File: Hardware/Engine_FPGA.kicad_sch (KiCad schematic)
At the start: 9 parts, among them J12 Conn_02x05_Odd_Even, SW1 SW_DS01-254, U16 AT40K10-2DQU, U2 AT40K10-2DQU

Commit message: Started fixing many small issues.
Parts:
- removed U16: AT40K10-2DQU, Package_QFP:PQFP-208_28x28mm_P0.5mm, symbol LRJ-parts:AT40K10-2DQU
- added U3: AT40K10-2DQU, Package_QFP:PQFP-208_28x28mm_P0.5mm, symbol LRJ-parts:AT40K10-2DQU
- renumbered J12 to J-fpga1
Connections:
- net ~{MCAS0} is gone; now on net ~{RFSH}: U2.111 (IO99)
- net ~{MCAS1} is gone; now on net ~{WAIT}: U2.112 (IO100)
- net ~{MCAS2} is gone; now on net ~{M1}: U2.114 (IO104)
- net ~{MCAS3} is gone; now on net ~{IORQ}: U2.115 (IO105)
- net ~{MRAS0} is gone; now on net Z80M: U2.116 (IO106)
- net ~{MRAS1} is gone; now on net ~{SLTSL1}: U2.117 (IO107)
- net ~{MRAS2} is gone; now on net ~{REDWC}: U2.163 (IO147)
- net ~{MRAS3} is gone; now on net ~{INDEX}: U2.164 (IO148)
- net ~{MREQ} is gone; now on net ~{STROBE}: U2.93 (IO89)
- net A17: now also U3.161 (IO145/A0); no longer U2.5 (IO2/A17)
- net A18: now also U3.162 (IO146/GCK7/A1); no longer U2.8 (IO5/A18)
- net A19: now also U3.165 (IO149/~{CS1}/A2); no longer U2.9 (IO6/A19)
- net A20: now also U3.166 (IO150/A3); no longer U2.17 (IO15/A20)
- net A21: now also U3.174 (IO161/A4); no longer U2.18 (IO16/A21)
- net A22: now also U3.175 (IO162/A5); no longer U2.23 (IO23/A22)
- net A23: now also U3.180 (IO167/A6); no longer U2.24 (IO24/A23)
- net A24: now also U3.181 (IO168/A7)
- net A25: now also U3.184 (IO169/A8)
- net A26: now also U3.185 (IO170/A9)
- net A27: now also U3.190 (IO175/A10)
- net A28: now also U3.191 (IO176/A11)
- net A29: now also U3.199 (IO185/A12)
- net A30: now also U3.200 (IO186/A13)
- net A31: now also U3.203 (IO191/A14)
- net CAPS_LED: now also U2.28 (IO26); no longer U2.32 (IO30)
- net CC1/HPD: now also U3.24 (IO24/A23)
- net CCLK: now also U3.153 (CCLK)
- net COL0: now also U2.32 (IO30); no longer U2.38 (IO39)
- net COL1: now also U2.33 (IO33); no longer U2.39 (IO40)
- net COL2: now also U2.34 (IO34); no longer U2.40 (IO41)
- net COL3: now also U2.35 (IO35); no longer U2.41 (IO42)
- net COL4: now also U2.38 (IO39); no longer U2.42 (IO43)
- net COL5: now also U2.39 (IO40); no longer U2.43 (IO44)
- net COL6: now also U2.40 (IO41); no longer U2.44 (IO45)
- net COL7: now also U2.41 (IO42); no longer U2.45 (IO46)
- net D0: now also U3.151 (IO143/D0)
- net D1: now also U3.147 (IO139/D1)
- net D10: now also U3.95 (IO91/D10)
- net D11: now also U3.87 (IO82/D11)
- net D12: now also U3.86 (IO81/D12)
- net D13: now also U3.81 (IO74/D13)
- net D14: now also U3.80 (IO73/D14)
- net D15: now also U3.76 (IO71/D15)
- net D2: now also U3.138 (IO127/D2)
- net D3: now also U3.132 (IO121/D3)
- net D4: now also U3.128 (IO119/D4)
- net D5: now also U3.122 (IO113/D5)
- net D6: now also U3.113 (IO103/D6)
- net D7: now also U3.109 (IO97/D7)
- net D8: now also U3.99 (IO95/D8)
- net D9: now also U3.96 (IO92/D9)
- net ENG_M0: now also U3.50 (M0)
- net ENG_M1: now also U3.48 (M1)
- net ENG_M2: now also U3.56 (M2)
- net I2C_AD1: now also U3.188 (IO173); no longer U2.28 (IO26)
- net I2C_AD2: now also U3.189 (IO174); no longer U2.29 (IO27)
- net I2C_AD3: now also U3.192 (IO179); no longer U2.30 (IO28)
- net I2C_AD4: now also U3.193 (IO180); no longer U2.27 (IO25)
- net I2C_SCL: now also U3.186 (IO171); no longer U2.89 (IO84)
- net I2C_SDA: now also U3.187 (IO172); no longer U2.91 (IO87)
- net INIT: now also U3.77 (IO72/INIT)
- net JOY_OUT_A: now also U3.118 (IO108)
- net JOY_OUT_B: now also U3.134 (IO123)
- net KANA_LED: now also U2.31 (IO29); no longer U2.35 (IO35)
- net KEY_CLICK: now also U2.29 (IO27); no longer U2.33 (IO33)
- net KEY_DIR: now also U2.27 (IO25); no longer U2.31 (IO29)
- net MCKE0: now also U3.172 (IO157)
- net MCKE1: now also U3.173 (IO158)
- net MD0: now also U3.6 (IO3)
- net MD1: now also U3.7 (IO4)
- net MD10: now also U3.22 (IO22)
- net MD11: now also U3.27 (IO25)
- net MD12: now also U3.28 (IO26)
- net MD13: now also U3.29 (IO27)
- net MD14: now also U3.30 (IO28)
- net MD15: now also U3.31 (IO29)
- net MD16: now also U3.32 (IO30)
- net MD17: now also U3.33 (IO33)
- net MD18: now also U3.34 (IO34)
- net MD19: now also U3.35 (IO35)
- net MD2: now also U3.10 (IO7)
- net MD20: now also U3.38 (IO39)
- net MD21: now also U3.39 (IO40)
- net MD22: now also U3.40 (IO41)
- net MD23: now also U3.41 (IO42)
- net MD24: now also U3.42 (IO43)
- net MD25: now also U3.43 (IO44)
- net MD26: now also U3.44 (IO45)
- net MD27: now also U3.45 (IO46)
- net MD28: now also U3.46 (IO47/OTS)
- net MD29: now also U3.58 (IO50/HDC)
- net MD3: now also U3.11 (IO8)
- net MD30: now also U3.59 (IO51)
- net MD31: now also U3.60 (IO52)
- net MD4: now also U3.12 (IO9)
- net MD5: now also U3.13 (IO10)
- net MD6: now also U3.16 (IO14)
- net MD7: now also U3.19 (IO19)
- net MD8: now also U3.20 (IO20)
- net MD9: now also U3.21 (IO21)
- net PAL_CLK_OUT: now also U2.47 (IO48/GCK2); no longer U2.36 (IO36/FCK2)
- net PD0: now also U2.75 (IO70)
- net PD1: now also U2.82 (IO75)
- net PD2: now also U2.83 (IO76)
- net PD3: now also U2.84 (IO77)
- net PD4: now also U2.85 (IO78)
- net PD5: now also U2.88 (IO83)
- net PD6: now also U2.89 (IO84)
- net PD7: now also U2.91 (IO87)
- net PRT_BUSY: now also U2.92 (IO88)
- net SD_CLK: now also U3.144 (IO136); no longer U2.85 (IO78)
- net SD_CMD: now also U3.143 (IO135); no longer U2.84 (IO77)
- net SD_DAT1: now also U3.137 (IO126); no longer U2.75 (IO70)
- net SD_DAT3: now also U3.140 (IO129); no longer U2.83 (IO76)
- net SD_DET_A: now also U3.146 (IO138); no longer U2.61 (IO53)
- net SD_DET_B: now also U3.148 (IO140); no longer U2.62 (IO54/LDC)
- net SD_MISO/DAT0: now also U3.145 (IO137); no longer U2.88 (IO83)
- net SD_MOSI/DAT2: now also U3.139 (IO128); no longer U2.82 (IO75)
- net SLT_DIR: now also U2.135 (IO124); no longer U2.92 (IO88)
- net SUP_INT: now also U2.143 (IO135); no longer U2.198 (IO184)
- net SWDCLK/RX1-: now also U3.9 (IO6/A19)
- net SWDIO/RX1+: now also U3.17 (IO15/A20)
- net SWO/RX2-: now also U3.18 (IO16/A21)
- net TSTCLK: now also U3.159 (TSTCLK)
- net USB1_D+: now also U3.110 (IO98/GCK5)
- net USB1_D-: now also U3.100 (IO96/GCK4)
- net USB2_D+: now also U3.36 (IO36/FCK2)
- net USB2_D-: now also U3.15 (IO13/FCK1)
- net Z80M: no longer U2.126 (IO117)
- net nRESET/RX2+: now also U3.23 (IO23/A22)
- net ~{BCK_A}: now also U3.112 (IO100)
- net ~{BCK_B}: now also U3.124 (IO115)
- net ~{BUSDIR1}: now also U2.118 (IO108); no longer U2.129 (IO120)
- net ~{BUSDIR2}: now also U2.124 (IO115); no longer U2.135 (IO124)
- net ~{BUSDIR3}: now also U2.126 (IO117); no longer U2.137 (IO126)
- net ~{CAS0}: now also U3.178 (IO165); no longer U2.140 (IO129)
- net ~{CHECK}: now also U3.133 (IO122/~{CHECK})
- net ~{CON}: now also U3.103 (~{CON})
- net ~{DIR}: now also U2.172 (IO157); no longer U2.176 (IO163)
- net ~{DRVSA}: now also U2.168 (IO154); no longer U2.170 (IO156)
- net ~{DRVSB}: now also U2.169 (IO155); no longer U2.172 (IO157)
- net ~{DSKCHG}: now also U2.188 (IO173); no longer U2.192 (IO179)
- net ~{FWD_A}: now also U3.111 (IO99)
- net ~{FWD_B}: now also U3.121 (IO112)
- net ~{INDEX}: no longer U2.168 (IO154)
- net ~{IORQ}: no longer U2.125 (IO116)
- net ~{KBD_WAIT}: now also U2.30 (IO28); no longer U2.34 (IO34)
- net ~{LFT_A}: now also U3.114 (IO104)
- net ~{LFT_B}: now also U3.125 (IO116)
- net ~{M1}: no longer U2.124 (IO115)
- net ~{MOTEA}: now also U2.167 (IO153); no longer U2.169 (IO155)
- net ~{MOTEB}: now also U2.170 (IO156); no longer U2.173 (IO158)
- net ~{MSIZE}: now also U3.179 (IO166); no longer U2.144 (IO136)
- net ~{OE_VT}: now also U2.140 (IO129); no longer U2.197 (IO183)
- net ~{PSG_CS}: now also U2.42 (IO43); no longer U2.46 (IO47/OTS)
- net ~{RAS0}: now also U3.176 (IO163); no longer U2.195 (IO181)
- net ~{RAS1}: now also U3.177 (IO164); no longer U2.143 (IO135)
- net ~{RDATA}: now also U2.186 (IO171); no longer U2.188 (IO173)
- net ~{RD}: now also U2.137 (IO126), U3.123 (IO114/CS0), U3.135 (IO124); no longer U2.149 (IO141)
- net ~{REDWC}: no longer U2.167 (IO153)
- net ~{RESET}: now also U3.108 (~{RESET})
- net ~{RFSH}: no longer U2.118 (IO108)
- net ~{RGT_A}: now also U3.115 (IO105)
- net ~{RGT_B}: now also U3.126 (IO117)
- net ~{ROM_A_EN}: now also U2.144 (IO136); no longer U2.139 (IO128)
- net ~{ROM_CS}: now also U2.43 (IO44); no longer U2.196 (IO182)
- net ~{SIDE1}: now also U2.187 (IO172); no longer U2.189 (IO174)
- net ~{SLTSL1}: no longer U2.127 (IO118)
- net ~{SLTSL2}: now also U2.121 (IO112); no longer U2.134 (IO123)
- net ~{SLTSL3}: now also U2.125 (IO116); no longer U2.136 (IO125)
- net ~{SLT_RST}: now also U2.136 (IO125); no longer U2.58 (IO50/HDC)
- net ~{Step}: now also U2.173 (IO158); no longer U2.177 (IO164)
- net ~{TRG1_A}: now also U3.116 (IO106)
- net ~{TRG1_B}: now also U3.127 (IO118)
- net ~{TRG2_A}: now also U3.117 (IO107)
- net ~{TRG2_B}: now also U3.129 (IO120)
- net ~{TRK00}: now also U2.178 (IO165); no longer U2.186 (IO171)
- net ~{WAIT}: no longer U2.121 (IO112)
- net ~{WDATA}: now also U2.176 (IO163); no longer U2.178 (IO165)
- net ~{WGATE}: now also U2.177 (IO164); no longer U2.179 (IO166)
- net ~{WPT}: now also U2.179 (IO166); no longer U2.187 (IO172)
- net ~{WR}: now also U2.139 (IO128), U3.136 (IO125); no longer U2.150 (IO142)
- net GND2 renamed GND
- net SMDAT1 renamed MID_RX
- net SMDAT2 renamed MID_TX
- net SMDAT3 renamed VID_ID
- net ~{CS12} renamed ~{ROM_A_WE}
- net ~{CS1} renamed ~{ROM_A_OE}
- net ~{CS2} renamed FanSen3
- new net DQMB0: U3.195 (IO181)
- new net DQMB1: U3.196 (IO182)
- new net DQMB2: U3.197 (IO183)
- new net DQMB3: U3.198 (IO184)
- new net DQMB4: U3.201 (IO189)
- new net DQMB5: U3.202 (IO190)
- new net DQMB6: U3.149 (IO141)
- new net DQMB7: U3.150 (IO142)
- new net FanCtrl1: U2.195 (IO181)
- new net FanCtrl2: U2.196 (IO182)
- new net FanCtrl3: U2.197 (IO183)
- new net FanSen1: U2.189 (IO174)
- new net FanSen2: U2.192 (IO179)
- new net HDD_PWM: U2.150 (IO142)
- new net I2C_AD5: U3.204 (IO192/GCK8/A15)
- new net MCLK0: U3.120 (IO111/FCK3)
- new net MCLK1: U3.141 (IO130/FCK4)
- new net MD32: U3.61 (IO53)
- new net MD33: U3.62 (IO54/LDC)
- new net MD34: U3.63 (IO55)
- new net MD35: U3.64 (IO56)
- new net MD36: U3.65 (IO57)
- new net MD37: U3.66 (IO58)
- new net MD38: U3.68 (IO61)
- new net MD39: U3.69 (IO62)
- new net MD40: U3.70 (IO63)
- new net MD41: U3.71 (IO64)
- new net MD42: U3.72 (IO65)
- new net MD43: U3.73 (IO66)
- new net MD44: U3.74 (IO69)
- new net MD45: U3.75 (IO70)
- new net MD46: U3.82 (IO75)
- new net MD47: U3.83 (IO76)
- new net MD48: U3.84 (IO77)
- new net MD49: U3.85 (IO78)
- new net MD50: U3.88 (IO83)
- new net MD51: U3.89 (IO84)
- new net MD52: U3.91 (IO87)
- new net MD53: U3.92 (IO88)
- new net MD54: U3.93 (IO89)
- new net MD55: U3.94 (IO90)
- new net MD56: U3.97 (IO93)
- new net MD57: U3.98 (IO94)
- new net MD58: U3.163 (IO147)
- new net MD59: U3.164 (IO148)
- new net MD60: U3.167 (IO153)
- new net MD61: U3.168 (IO154)
- new net MD62: U3.169 (IO155)
- new net MD63: U3.170 (IO156)
- new net ~{BHEN}: U3.5 (IO2/A17)
- new net ~{BLEN}: U3.8 (IO5/A18)
- new net ~{RY_BY}: U2.149 (IO141)
- new net ~{SLT_CS12}: U2.129 (IO120)
- new net ~{SLT_CS1}: U2.127 (IO118)
- new net ~{SLT_CS2}: U2.134 (IO123)
- no-connect marks 63 -> 24
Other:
- note added: "AT40K programming-pins: ----------------- DO (data out) CHECK CON INIT/ERR CI (clock in) CO (clock out) VCC (VTref) GND N/C Optional: CSOUT ~{CHECK}"
- note added: "Cooling Fans"
- note added: "Floppy drive: https://github.com/SukkoPera/OpenFlops (Issue! MCU-based, not HDL-based)"
- note added: "Front panel"
- note added: "MIDI audio"
- note added: "MSX-engine chips: ------------ *PPI* ---- v- 7400 (four 2-input NAND) v- 7430 (x2) (8-input NAND) v- 7432 (x3) (four 2-input OR) v- 74273 (x2) (eight D-type flip-flop with reset; positive-edge trigger) -74540 (Octal buffer/line driver; inverting) -74541 (x3) (8-bit Buffer/Line Driver) v- 74153 (x2) (two 4-input multiplexer) v- 8255 Logic: 7x2 NAND + 4 NAND (18 NAND) 4x3 OR (36 NAND) 8x2 Flip-flop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"
- note added: "Memory"
- note added: "Memory Masking"
- note added: "Memory module"
- note added: "Tips: ------- 1. Specify different Resets? Reset-design: https://semiengineering.com/respecting-reset/"
- note added: "USB-JTAG(SW): --------- RX1- = SWDCLK RX1+ = SWDIO RX2- = SWO RX2+ = nReSeT SBU1 = VCC(target) SBU2 = GND JTAG-JTAG(SW): ---------- SWDCLK = TCK SWDIO = TMS SWO = TDO nReSeT = TRST"
- note added: "USB-chips R5F10JGCAFB#V0 NUC123LD4AN0"
- note added: "VTO - voltage Controlled Oscillator -------- Frequencies needed: 80 MHz (FPGA) 25.175 MHz (VGA) 18.432 MHz (CPU) 4.43361875 MHz (PAL) 3.579545 MHz (NTSC)"
- note added: "control"
- note removed: "CSOUT(clk_psg)"
- note removed: "DO (data out) CHECK CON INIT/ERR CI (clock in) CO (clock out) VCC (VTref) GND N/C"
- note removed: "MSX-engine chips: ------------ PPI ---- v- 7400 (four 2-input NAND) v- 7430 (x2) (8-input NAND) v- 7432 (x3) (four 2-input OR) v- 74273 (x2) (eight D-type flip-flop with reset; positive-edge trigger) -74540 (Octal buffer/line driver; inverting) -74541 (x3) (8-bit Buffer/Line Driver) v- 74153 (x2) (two 4-input multiplexer) v- 8255 Logic: 7x2 NAND + 4 NAND (18 NAND) 4x3 OR (36 NAND) 8x2 Flip-flop (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"
- note removed: "Optional:"
- note removed: "USB-JTAG: --------- RX1- = SWDCLK RX1+ = SWDIO RX2- = SWO RX2+ = nReSeT SBU1 = VCC(target) SBU2 = GND"
- note removed: "~{CHECK}"
- moved on the sheet: U2A, U2B, U2G

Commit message: Added a 3D-model for the SDRAM-module. Prepping the design for a fork using a single, more modern FPGA.
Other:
- moved on the sheet: U3C, U3D, U3E, U3F, U3G

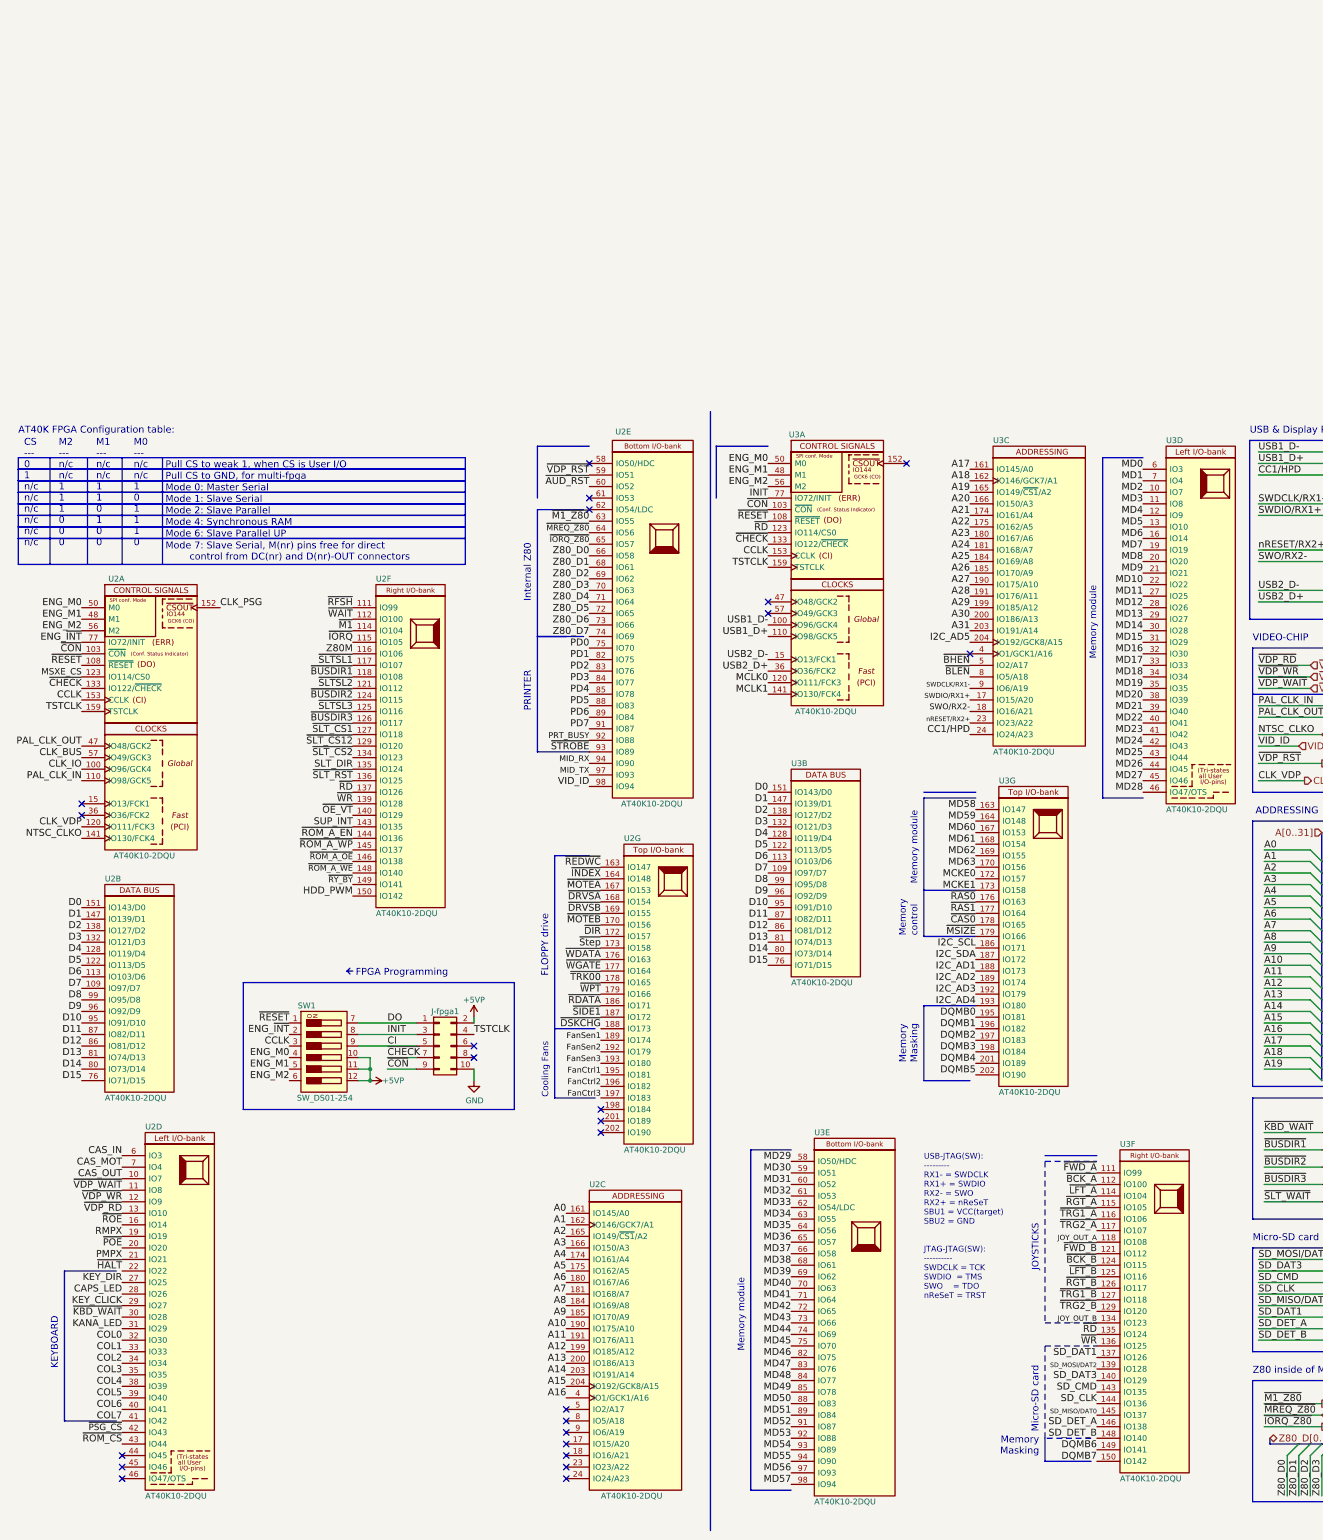
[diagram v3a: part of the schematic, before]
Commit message: Many tweaks and changes, such as a slight redesign of the VDP-baord.
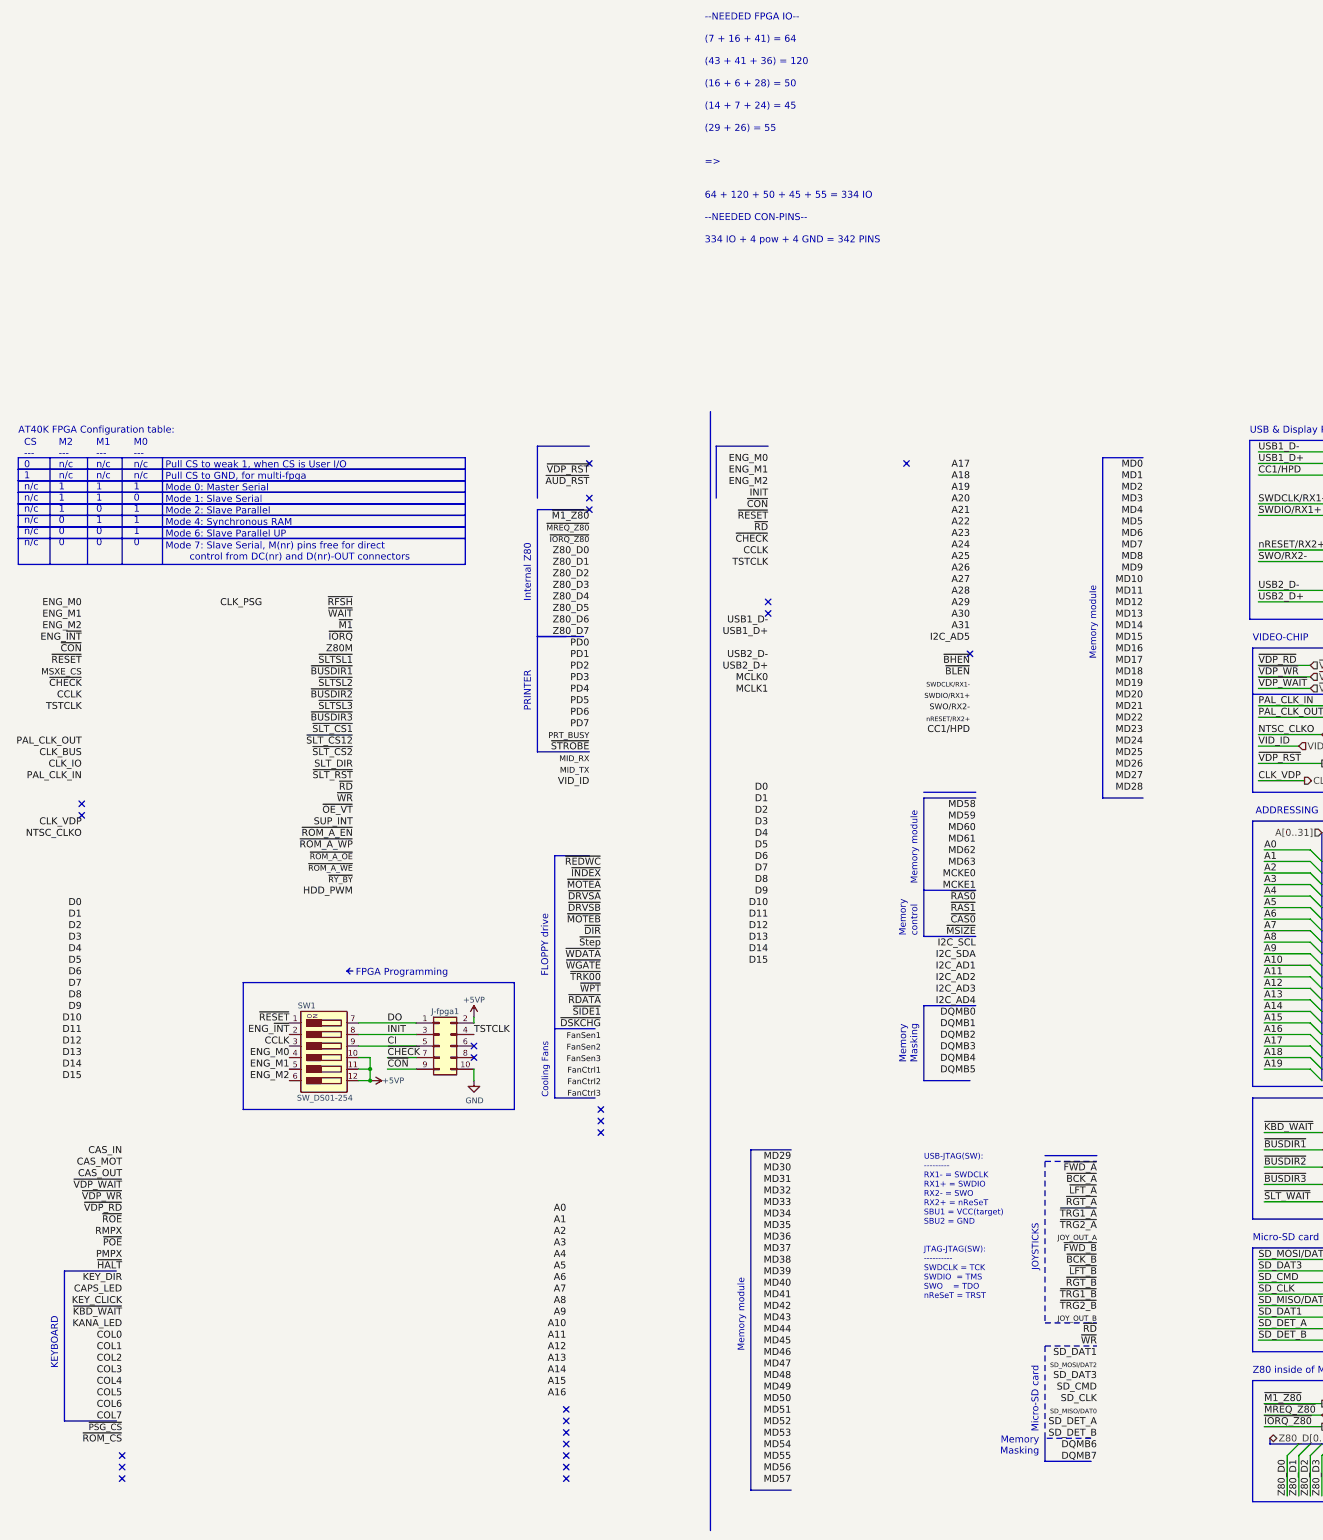
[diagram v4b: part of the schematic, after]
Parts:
- removed U2, U3: AT40K10-2DQU, Package_QFP:PQFP-208_28x28mm_P0.5mm, symbol LRJ-parts:AT40K10-2DQU
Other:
- note added: "--NEEDED FPGA IO-- (7 + 16 + 41) = 64 (43 + 41 + 36) = 120 (16 + 6 + 28) = 50 (14 + 7 + 24) = 45 (29 + 26) = 55 => 64 + 120 + 50 + 45 + 55 = 334 IO --NEEDED CON-PINS-- 334 IO + 4 pow + 4 GND = 342 PINS"

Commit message: Returned to Simm-72 memory module to simplify design, returned to AT40K40 with 254 io, FPGA.
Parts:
- added U2: AT40K40-2FQC, LRJ:PQFP-304_40x40mm_P0.5mm, symbol LRJ-parts:AT40K40-2FQC
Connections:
- net A0: now also U2.74 (IO193/A0)
- net A1: now also U2.73 (IO194/GCK7/A1)
- net A10: now also U2.31 (IO231/A10)
- net A11: now also U2.30 (IO232/A11)
- net A12: now also U2.12 (IO247/A12)
- net A13: now also U2.10 (IO248/A13)
- net A14: now also U2.3 (IO255/A14)
- net A15: now also U2.2 (IO256/GCK8/A15)
- net A16: now also U2.303 (IO1/A16)
- net A17: now also U2.302 (IO2/A17)
- net A18: now also U2.299 (IO5/A18)
- net A19: now also U2.298 (IO6/A19)
- net A2: now also U2.70 (IO197/~{CS1}/A2)
- net A20: now also U2.284 (IO19/A20)
- net A21: now also U2.283 (IO20/A21)
- net A22: now also U2.270 (IO31/A22)
- net A23: now also U2.269 (IO32/A23)
- net A24: now also U2.34 (IO228)
- net A25: now also U2.33 (IO229)
- net A26: now also U2.32 (IO230)
- net A27: now also U2.29 (IO233)
- net A28: now also U2.28 (IO234)
- net A29: now also U2.27 (IO235)
- net A3: now also U2.69 (IO198/A3)
- net A30: now also U2.26 (IO236)
- net A31: now also U2.23 (IO237)
- net A4: now also U2.47 (IO217/A4)
- net A5: now also U2.46 (IO218/A5)
- net A6: now also U2.41 (IO223/A6)
- net A7: now also U2.40 (IO224/A7)
- net A8: now also U2.37 (IO225/A8)
- net A9: now also U2.36 (IO226/A9)
- net CAPS_LED: now also U2.56 (IO210)
- net CAS_IN: now also U2.72 (IO195)
- net CAS_MOT: now also U2.71 (IO196)
- net CAS_OUT: now also U2.68 (IO199)
- net CC1/HPD: now also U2.185 (IO101)
- net CCLK: now also U2.78 (CCLK)
- net CLK_BUS: now also U2.226 (IO65/GCK3)
- net CLK_IO: now also U2.155 (IO128/GCK4)
- net CLK_PSG: now also U2.79 (IO192/GCK6/~{CSOUT})
- net CLK_VDP: now also U2.131 (IO147/FCK3)
- net COL0: now also U2.50 (IO214)
- net COL1: now also U2.49 (IO215)
- net COL2: now also U2.48 (IO216)
- net COL3: now also U2.45 (IO219)
- net COL4: now also U2.44 (IO220)
- net COL5: now also U2.43 (IO221)
- net COL6: now also U2.42 (IO222)
- net COL7: now also U2.35 (IO227)
- net D0: now also U2.80 (IO191/D0)
- net D1: now also U2.86 (IO185/D1)
- net D10: now also U2.160 (IO123/D10)
- net D11: now also U2.174 (IO110/D11)
- net D12: now also U2.175 (IO109/D12)
- net D13: now also U2.188 (IO98/D13)
- net D14: now also U2.189 (IO97/D14)
- net D15: now also U2.193 (IO95/D15)
- net D2: now also U2.103 (IO171/D2)
- net D3: now also U2.113 (IO161/D3)
- net D4: now also U2.117 (IO159/D4)
- net D5: now also U2.127 (IO149/D5)
- net D6: now also U2.142 (IO137/D6)
- net D7: now also U2.150 (IO129/D7)
- net D8: now also U2.156 (IO127/D8)
- net D9: now also U2.159 (IO124/D9)
- net ENG_M0: now also U2.229 (M0)
- net ENG_M1: now also U2.231 (M1)
- net ENG_M2: now also U2.227 (M2)
- net ENG_~{INT}: now also U2.192 (INIT/IO96)
- net FanCtrl1: now also U2.241 (IO55)
- net FanCtrl2: now also U2.240 (IO56)
- net FanCtrl3: now also U2.239 (IO57)
- net FanSen1: now also U2.244 (IO52)
- net FanSen2: now also U2.243 (IO53)
- net FanSen3: now also U2.242 (IO54)
- net HDD_PWM: now also U2.264 (IO35)
- net I2C_AD1: now also U2.163 (IO120)
- net I2C_AD2: now also U2.162 (IO121)
- net I2C_AD3: now also U2.161 (IO122)
- net I2C_AD4: now also U2.158 (IO125)
- net I2C_AD5: now also U2.157 (IO126)
- net I2C_SCL: now also U2.165 (IO118)
- net I2C_SDA: now also U2.164 (IO119)
- net JOY_OUT_A: now also U2.15 (IO244)
- net JOY_OUT_B: now also U2.5 (IO253)
- net KANA_LED: now also U2.51 (IO213)
- net KEY_CLICK: now also U2.55 (IO211)
- net KEY_DIR: now also U2.57 (IO209)
- net MD0: now also U2.148 (IO131)
- net MD1: now also U2.147 (IO132)
- net MD10: now also U2.135 (IO144)
- net MD11: now also U2.133 (IO145)
- net MD12: now also U2.132 (IO146)
- net MD13: now also U2.130 (IO148)
- net MD14: now also U2.125 (IO151)
- net MD15: now also U2.124 (IO152)
- net MD16: now also U2.123 (IO153)
- net MD17: now also U2.122 (IO154)
- net MD18: now also U2.121 (IO155)
- net MD19: now also U2.120 (IO156)
- net MD2: now also U2.146 (IO135)
- net MD20: now also U2.119 (IO157)
- net MD21: now also U2.118 (IO158)
- net MD22: now also U2.116 (IO160)
- net MD23: now also U2.111 (IO163)
- net MD24: now also U2.110 (IO164)
- net MD25: now also U2.109 (IO165)
- net MD26: now also U2.108 (IO166)
- net MD27: now also U2.107 (IO167)
- net MD28: now also U2.106 (IO168)
- net MD29: now also U2.105 (IO169)
- net MD3: now also U2.145 (IO136)
- net MD30: now also U2.104 (IO170)
- net MD31: now also U2.102 (IO171)
- net MD4: now also U2.141 (IO138)
- net MD5: now also U2.140 (IO139)
- net MD6: now also U2.139 (IO140)
- net MD7: now also U2.138 (IO141)
- net MD8: now also U2.137 (IO142)
- net MD9: now also U2.136 (IO143)
- net MID_RX: now also U2.238 (IO58)
- net MID_TX: now also U2.237 (IO59)
- net MSXE_CS: now also U2.126 (CS0/IO150)
- net NTSC_CLKO: now also U2.98 (IO174/FCK4)
- net PAL_CLK_IN: now also U2.149 (IO130/GCK5)
- net PAL_CLK_OUT: now also U2.232 (IO64/GCK2)
- net PD0: now also U2.209 (IO81)
- net PD1: now also U2.208 (IO82)
- net PD2: now also U2.207 (IO83)
- net PD3: now also U2.206 (IO84)
- net PD4: now also U2.203 (IO85)
- net PD5: now also U2.202 (IO86)
- net PD6: now also U2.201 (IO87)
- net PD7: now also U2.200 (IO88)
- net PMPX: now also U2.60 (IO207)
- net PRT_BUSY: now also U2.199 (IO89)
- net RMPX: now also U2.62 (IO205)
- net SD_CLK: now also U2.169 (IO114)
- net SD_CMD: now also U2.170 (IO113)
- net SD_DAT1: now also U2.178 (IO108)
- net SD_DAT3: now also U2.172 (IO112)
- net SD_DET_A: now also U2.167 (IO116)
- net SD_DET_B: now also U2.166 (IO117)
- net SD_MISO/DAT0: now also U2.168 (IO115)
- net SD_MOSI/DAT2: now also U2.173 (IO111)
- net SLT_DIR: now also U2.279 (IO22)
- net SUP_INT: now also U2.274 (IO27)
- net SWDCLK/RX1-: now also U2.195 (IO93)
- net SWDIO/RX1+: now also U2.194 (IO94)
- net SWO/RX2-: now also U2.187 (IO99)
- net TSTCLK: now also U2.76 (TSTCLK)
- net USB1_D+: now also U2.183 (IO103)
- net USB1_D-: now also U2.184 (IO102)
- net USB2_D+: now also U2.181 (IO105)
- net USB2_D-: now also U2.182 (IO104)
- net VID_ID: now also U2.236 (IO60)
- net Z80M: now also U2.295 (IO9)
- net Z80_D0: now also U2.220 (IO71)
- net Z80_D1: now also U2.219 (IO72)
- net Z80_D2: now also U2.218 (IO73)
- net Z80_D3: now also U2.217 (IO74)
- net Z80_D4: now also U2.216 (IO75)
- net Z80_D5: now also U2.215 (IO76)
- net Z80_D6: now also U2.214 (IO79)
- net Z80_D7: now also U2.213 (IO80)
- net nRESET/RX2+: now also U2.186 (IO100)
- net ~{AUD_RST}: now also U2.224 (IO67)
- net ~{BCK_A}: now also U2.21 (IO239)
- net ~{BCK_B}: now also U2.13 (IO246)
- net ~{BHEN}: now also U2.197 (IO91)
- net ~{BLEN}: now also U2.196 (IO92)
- net ~{BUSDIR1}: now also U2.293 (IO11)
- net ~{BUSDIR2}: now also U2.291 (IO13)
- net ~{BUSDIR3}: now also U2.289 (IO15)
- net ~{CAS0}: now also U2.96 (IO176)
- net ~{CHECK}: now also U2.112 (~{CHECK}/IO162)
- net ~{CON}: now also U2.153 (~{CON})
- net ~{DIR}: now also U2.257 (IO42)
- net ~{DRVSA}: now also U2.260 (IO39)
- net ~{DRVSB}: now also U2.259 (IO40)
- net ~{DSKCHG}: now also U2.245 (IO51)
- net ~{FWD_A}: now also U2.22 (IO238)
- net ~{FWD_B}: now also U2.14 (IO245)
- net ~{HALT}: now also U2.59 (IO208)
- net ~{INDEX}: now also U2.262 (IO37)
- net ~{IORQ_Z80}: now also U2.221 (IO70/LDC)
- net ~{IORQ}: now also U2.296 (IO8)
- net ~{KBD_WAIT}: now also U2.54 (IO212)
- net ~{LFT_A}: now also U2.20 (IO240)
- net ~{LFT_B}: now also U2.9 (IO249)
- net ~{M1_Z80}: now also U2.223 (IO68)
- net ~{M1}: now also U2.297 (IO7)
- net ~{MOTEA}: now also U2.261 (IO38)
- net ~{MOTEB}: now also U2.258 (IO41)
- net ~{MREQ_Z80}: now also U2.222 (IO69)
- net ~{MSIZE}: now also U2.92 (IO179)
- net ~{OE_VT}: now also U2.275 (IO26)
- net ~{POE}: now also U2.61 (IO206)
- net ~{PSG_CS}: now also U2.235 (IO61)
- net ~{RAS0}: now also U2.99 (IO173)
- net ~{RAS1}: now also U2.90 (IO181), U2.97 (IO175)
- net ~{RDATA}: now also U2.247 (IO49)
- net ~{RD}: now also U2.180 (IO106), U2.277 (IO24)
- net ~{REDWC}: now also U2.263 (IO36)
- net ~{RESET}: now also U2.151 (~{RESET})
- net ~{RFSH}: now also U2.301 (IO3)
- net ~{RGT_A}: now also U2.18 (IO241)
- net ~{RGT_B}: now also U2.8 (IO250)
- net ~{ROE}: now also U2.63 (IO204)
- net ~{ROM_A_EN}: now also U2.273 (IO28)
- net ~{ROM_A_OE}: now also U2.271 (IO30)
- net ~{ROM_A_WE}: now also U2.266 (IO33)
- net ~{ROM_A_WP}: now also U2.272 (IO29)
- net ~{ROM_CS}: now also U2.234 (IO62)
- net ~{RY_BY}: now also U2.265 (IO34)
- net ~{SIDE1}: now also U2.246 (IO50)
- net ~{SLTSL1}: now also U2.294 (IO10)
- net ~{SLTSL2}: now also U2.292 (IO12)
- net ~{SLTSL3}: now also U2.290 (IO14)
- net ~{SLT_CS12}: now also U2.285 (IO18)
- net ~{SLT_CS1}: now also U2.288 (IO16)
- net ~{SLT_CS2}: now also U2.280 (IO21)
- net ~{SLT_RST}: now also U2.278 (IO23)
- net ~{STROBE}: now also U2.198 (IO90)
- net ~{Step}: now also U2.256 (IO43)
- net ~{TRG1_A}: now also U2.17 (IO242)
- net ~{TRG1_B}: now also U2.7 (IO251)
- net ~{TRG2_A}: now also U2.16 (IO243)
- net ~{TRG2_B}: now also U2.6 (IO252)
- net ~{TRK00}: now also U2.251 (IO46)
- net ~{VDP_RD}: now also U2.64 (IO203)
- net ~{VDP_RST}: now also U2.225 (IO66/HDC)
- net ~{VDP_WAIT}: now also U2.67 (IO200)
- net ~{VDP_WR}: now also U2.65 (IO202)
- net ~{WAIT}: now also U2.300 (IO4)
- net ~{WDATA}: now also U2.255 (IO44)
- net ~{WGATE}: now also U2.252 (IO45)
- net ~{WPT}: now also U2.250 (IO47)
- net ~{WR}: now also U2.179 (IO107), U2.276 (IO25)
- new net MPD1: U2.87 (IO184)
- new net MPD2: U2.85 (IO186)
- new net MPD3: U2.84 (IO187)
- new net MPD4: U2.83 (IO188)
- new net ~{CAS1}: U2.94 (IO177)
- new net ~{CAS2}: U2.93 (IO178)
- new net ~{CAS3}: U2.91 (IO180)
- new net ~{RAS2}: U2.89 (IO182)
- new net ~{RAS3}: U2.88 (IO183)
- no-connect marks 24 -> 3
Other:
- note added: "Turbo-R databuses: ----- Connected to System-IC Db1: Rom 4 MB, Floppy controller, expansion-slot, VDP Connected to System-IC Db2: R800 Connected to MSX-engine: YM2413, System-IC"
- note removed: "Memory Masking"
- moved on the sheet: J-fpga1, SW1
